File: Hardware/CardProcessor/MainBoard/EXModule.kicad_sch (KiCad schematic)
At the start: 1 part, among them J3 MEC5-140-01-L-DV-W1-K

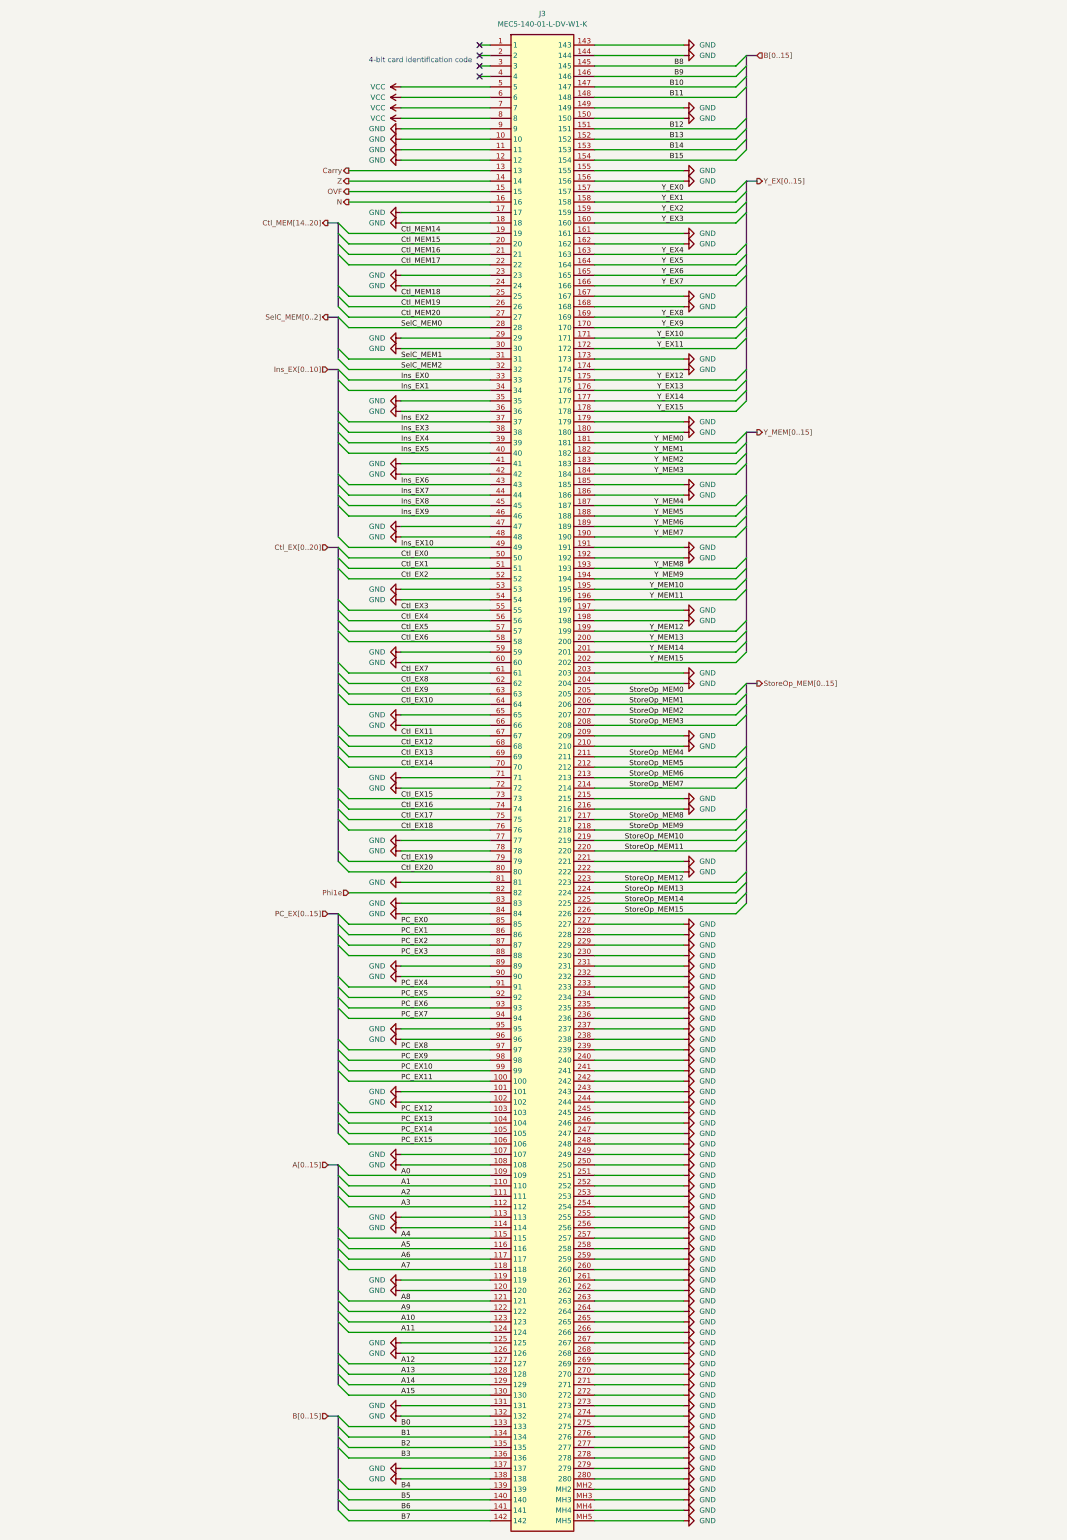
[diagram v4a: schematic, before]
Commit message: MainBoard: Rearrange slot connector pinout for easier PCB routing
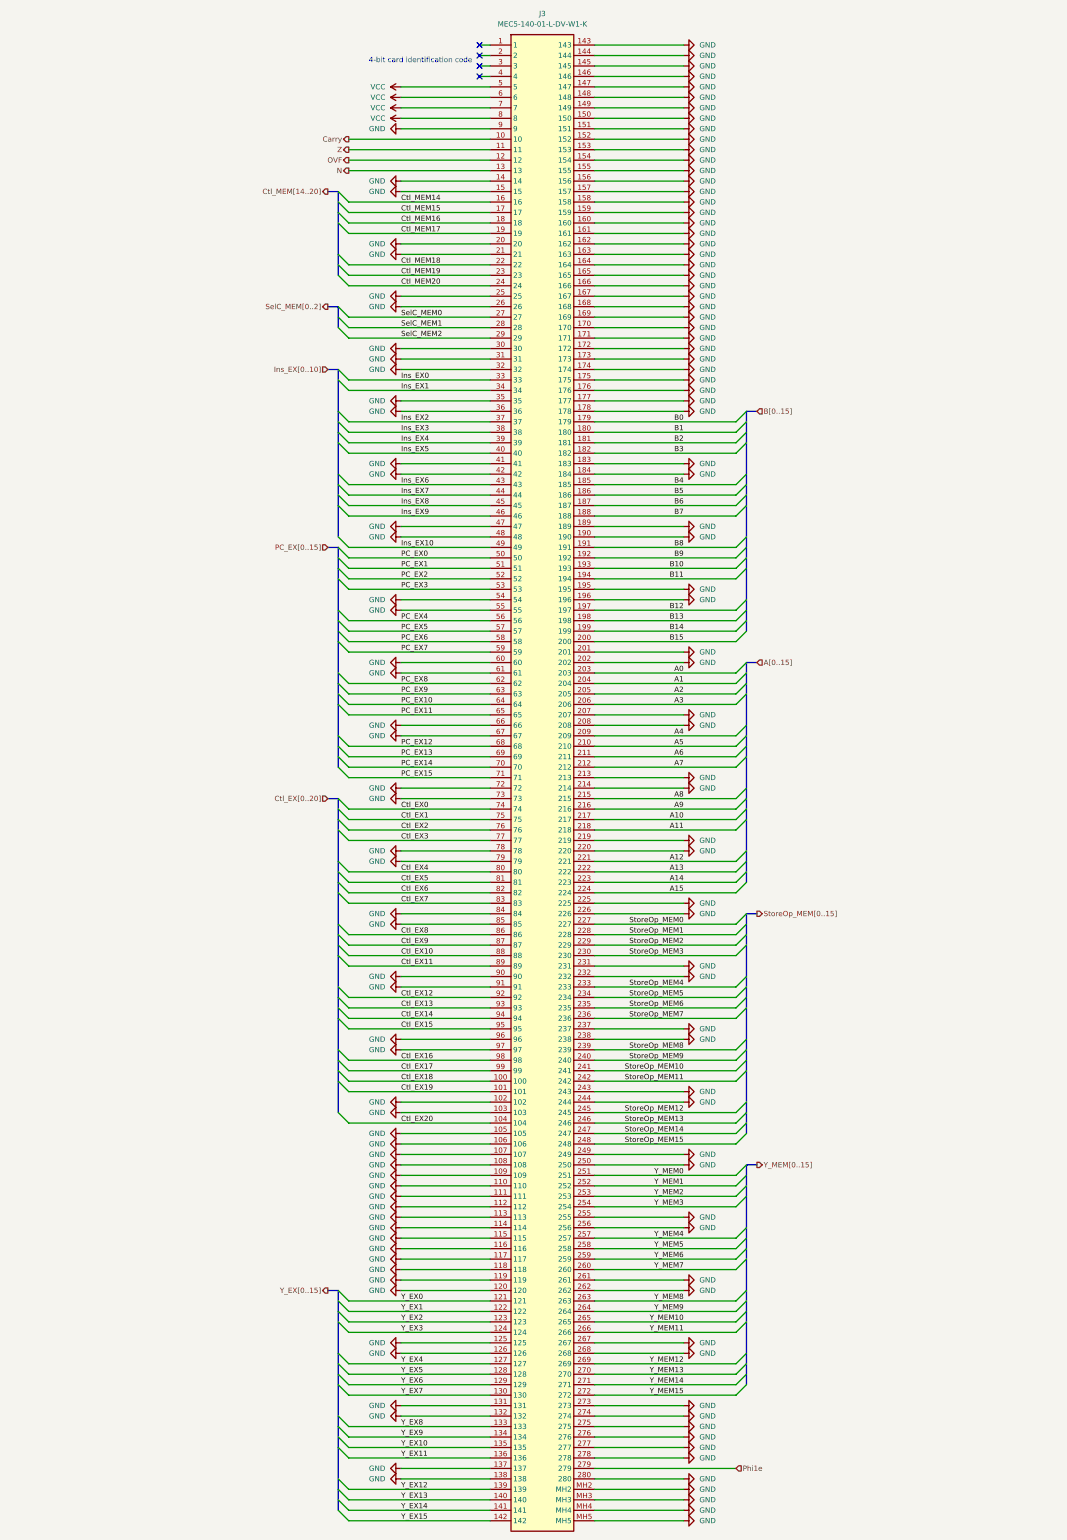
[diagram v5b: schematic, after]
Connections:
- net A0: now also J3.203; no longer J3.109
- net A1: now also J3.204; no longer J3.110
- net A10: now also J3.217; no longer J3.123
- net A11: now also J3.218; no longer J3.124
- net A12: now also J3.221; no longer J3.127
- net A13: now also J3.222; no longer J3.128
- net A14: now also J3.223; no longer J3.129
- net A15: now also J3.224; no longer J3.130
- net A2: now also J3.205; no longer J3.111
- net A3: now also J3.206; no longer J3.112
- net A4: now also J3.209; no longer J3.115
- net A5: now also J3.210; no longer J3.116
- net A6: now also J3.211; no longer J3.117
- net A7: now also J3.212; no longer J3.118
- net A8: now also J3.215; no longer J3.121
- net A9: now also J3.216; no longer J3.122
- net B0: now also J3.179; no longer J3.133
- net B1: now also J3.180; no longer J3.134
- net B10: now also J3.193; no longer J3.147
- net B11: now also J3.194; no longer J3.148
- net B12: now also J3.197; no longer J3.151
- net B13: now also J3.198; no longer J3.152
- net B14: now also J3.199; no longer J3.153
- net B15: now also J3.200; no longer J3.154
- net B2: now also J3.181; no longer J3.135
- net B3: now also J3.182; no longer J3.136
- net B4: now also J3.185; no longer J3.139
- net B5: now also J3.186; no longer J3.140
- net B6: now also J3.187; no longer J3.141
- net B7: now also J3.188; no longer J3.142
- net B8: now also J3.191; no longer J3.145
- net B9: now also J3.192; no longer J3.146
- net Carry: now also J3.10; no longer J3.13
- net Ctl_EX0: now also J3.74; no longer J3.50
- net Ctl_EX1: now also J3.75; no longer J3.51
- net Ctl_EX10: now also J3.88; no longer J3.64
- net Ctl_EX11: now also J3.89; no longer J3.67
- net Ctl_EX12: now also J3.92; no longer J3.68
- net Ctl_EX13: now also J3.93; no longer J3.69
- net Ctl_EX14: now also J3.94; no longer J3.70
- net Ctl_EX15: now also J3.95; no longer J3.73
- net Ctl_EX16: now also J3.98; no longer J3.74
- net Ctl_EX17: now also J3.99; no longer J3.75
- net Ctl_EX18: now also J3.100; no longer J3.76
- net Ctl_EX19: now also J3.101; no longer J3.79
- net Ctl_EX2: now also J3.76; no longer J3.52
- net Ctl_EX20: now also J3.104; no longer J3.80
- net Ctl_EX3: now also J3.77; no longer J3.55
- net Ctl_EX4: now also J3.80; no longer J3.56
- net Ctl_EX5: now also J3.81; no longer J3.57
- net Ctl_EX6: now also J3.82; no longer J3.58
- net Ctl_EX7: now also J3.83; no longer J3.61
- net Ctl_EX8: now also J3.86; no longer J3.62
- net Ctl_EX9: now also J3.87; no longer J3.63
- net Ctl_MEM14: now also J3.16; no longer J3.19
- net Ctl_MEM15: now also J3.17; no longer J3.20
- net Ctl_MEM16: now also J3.18; no longer J3.21
- net Ctl_MEM17: now also J3.19; no longer J3.22
- net Ctl_MEM18: now also J3.22; no longer J3.25
- net Ctl_MEM19: now also J3.23; no longer J3.26
- net Ctl_MEM20: now also J3.24; no longer J3.27
- net GND: now also J3.103, J3.105, J3.106, J3.109, J3.110, J3.111, J3.112, J3.115, J3.116, J3.117, J3.118, J3.14, J3.145, J3.146, J3.147, J3.148, J3.15, J3.151, J3.152, J3.153, J3.154, J3.157, J3.158, J3.159, J3.160, J3.163, J3.164, J3.165, J3.166, J3.169, J3.170, J3.171, J3.172, J3.175, J3.176, J3.177, J3.178, J3.183, J3.184, J3.189, J3.190, J3.195, J3.196, J3.20, J3.201, J3.202, J3.207, J3.208, J3.21, J3.213, J3.214, J3.219, J3.220, J3.225, J3.226, J3.25, J3.26, J3.31, J3.32, J3.55, J3.61, J3.67, J3.73, J3.79, J3.85, J3.91, J3.97; no longer J3.10, J3.101, J3.11, J3.12, J3.17, J3.179, J3.18, J3.180, J3.185, J3.186, J3.191, J3.192, J3.197, J3.198, J3.203, J3.204, J3.209, J3.210, J3.215, J3.216, J3.221, J3.222, J3.227, J3.228, J3.229, J3.23, J3.230, J3.233, J3.234, J3.235, J3.236, J3.239, J3.24, J3.240, J3.241, J3.242, J3.245, J3.246, J3.247, J3.248, J3.251, J3.252, J3.253, J3.254, J3.257, J3.258, J3.259, J3.260, J3.263, J3.264, J3.265, J3.266, J3.269, J3.270, J3.271, J3.272, J3.279, J3.29, J3.53, J3.59, J3.65, J3.71, J3.77, J3.81, J3.83, J3.89, J3.95
- net N: now also J3.13; no longer J3.16
- net OVF: now also J3.12; no longer J3.15
- net PC_EX0: now also J3.50; no longer J3.85
- net PC_EX1: now also J3.51; no longer J3.86
- net PC_EX10: now also J3.64; no longer J3.99
- net PC_EX11: now also J3.65; no longer J3.100
- net PC_EX12: now also J3.68; no longer J3.103
- net PC_EX13: now also J3.69; no longer J3.104
- net PC_EX14: now also J3.70; no longer J3.105
- net PC_EX15: now also J3.71; no longer J3.106
- net PC_EX2: now also J3.52; no longer J3.87
- net PC_EX3: now also J3.53; no longer J3.88
- net PC_EX4: now also J3.56; no longer J3.91
- net PC_EX5: now also J3.57; no longer J3.92
- net PC_EX6: now also J3.58; no longer J3.93
- net PC_EX7: now also J3.59; no longer J3.94
- net PC_EX8: now also J3.62; no longer J3.97
- net PC_EX9: now also J3.63; no longer J3.98
- net Phi1e: now also J3.279; no longer J3.82
- net SelC_MEM0: now also J3.27; no longer J3.28
- net SelC_MEM1: now also J3.28; no longer J3.31
- net SelC_MEM2: now also J3.29; no longer J3.32
- net StoreOp_MEM0: now also J3.227; no longer J3.205
- net StoreOp_MEM1: now also J3.228; no longer J3.206
- net StoreOp_MEM10: now also J3.241; no longer J3.219
- net StoreOp_MEM11: now also J3.242; no longer J3.220
- net StoreOp_MEM12: now also J3.245; no longer J3.223
- net StoreOp_MEM13: now also J3.246; no longer J3.224
- net StoreOp_MEM14: now also J3.247; no longer J3.225
- net StoreOp_MEM15: now also J3.248; no longer J3.226
- net StoreOp_MEM2: now also J3.229; no longer J3.207
- net StoreOp_MEM3: now also J3.230; no longer J3.208
- net StoreOp_MEM4: now also J3.233; no longer J3.211
- net StoreOp_MEM5: now also J3.234; no longer J3.212
- net StoreOp_MEM6: now also J3.235; no longer J3.213
- net StoreOp_MEM7: now also J3.236; no longer J3.214
- net StoreOp_MEM8: now also J3.239; no longer J3.217
- net StoreOp_MEM9: now also J3.240; no longer J3.218
- net Y_EX0: now also J3.121; no longer J3.157
- net Y_EX1: now also J3.122; no longer J3.158
- net Y_EX10: now also J3.135; no longer J3.171
- net Y_EX11: now also J3.136; no longer J3.172
- net Y_EX12: now also J3.139; no longer J3.175
- net Y_EX13: now also J3.140; no longer J3.176
- net Y_EX14: now also J3.141; no longer J3.177
- net Y_EX15: now also J3.142; no longer J3.178
- net Y_EX2: now also J3.123; no longer J3.159
- net Y_EX3: now also J3.124; no longer J3.160
- net Y_EX4: now also J3.127; no longer J3.163
- net Y_EX5: now also J3.128; no longer J3.164
- net Y_EX6: now also J3.129; no longer J3.165
- net Y_EX7: now also J3.130; no longer J3.166
- net Y_EX8: now also J3.133; no longer J3.169
- net Y_EX9: now also J3.134; no longer J3.170
- net Y_MEM0: now also J3.251; no longer J3.181
- net Y_MEM1: now also J3.252; no longer J3.182
- net Y_MEM10: now also J3.265; no longer J3.195
- net Y_MEM11: now also J3.266; no longer J3.196
- net Y_MEM12: now also J3.269; no longer J3.199
- net Y_MEM13: now also J3.270; no longer J3.200
- net Y_MEM14: now also J3.271; no longer J3.201
- net Y_MEM15: now also J3.272; no longer J3.202
- net Y_MEM2: now also J3.253; no longer J3.183
- net Y_MEM3: now also J3.254; no longer J3.184
- net Y_MEM4: now also J3.257; no longer J3.187
- net Y_MEM5: now also J3.258; no longer J3.188
- net Y_MEM6: now also J3.259; no longer J3.189
- net Y_MEM7: now also J3.260; no longer J3.190
- net Y_MEM8: now also J3.263; no longer J3.193
- net Y_MEM9: now also J3.264; no longer J3.194
- net Z: now also J3.11; no longer J3.14

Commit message: MainBoard: Change card slots' pinout to ease routing of the PCB
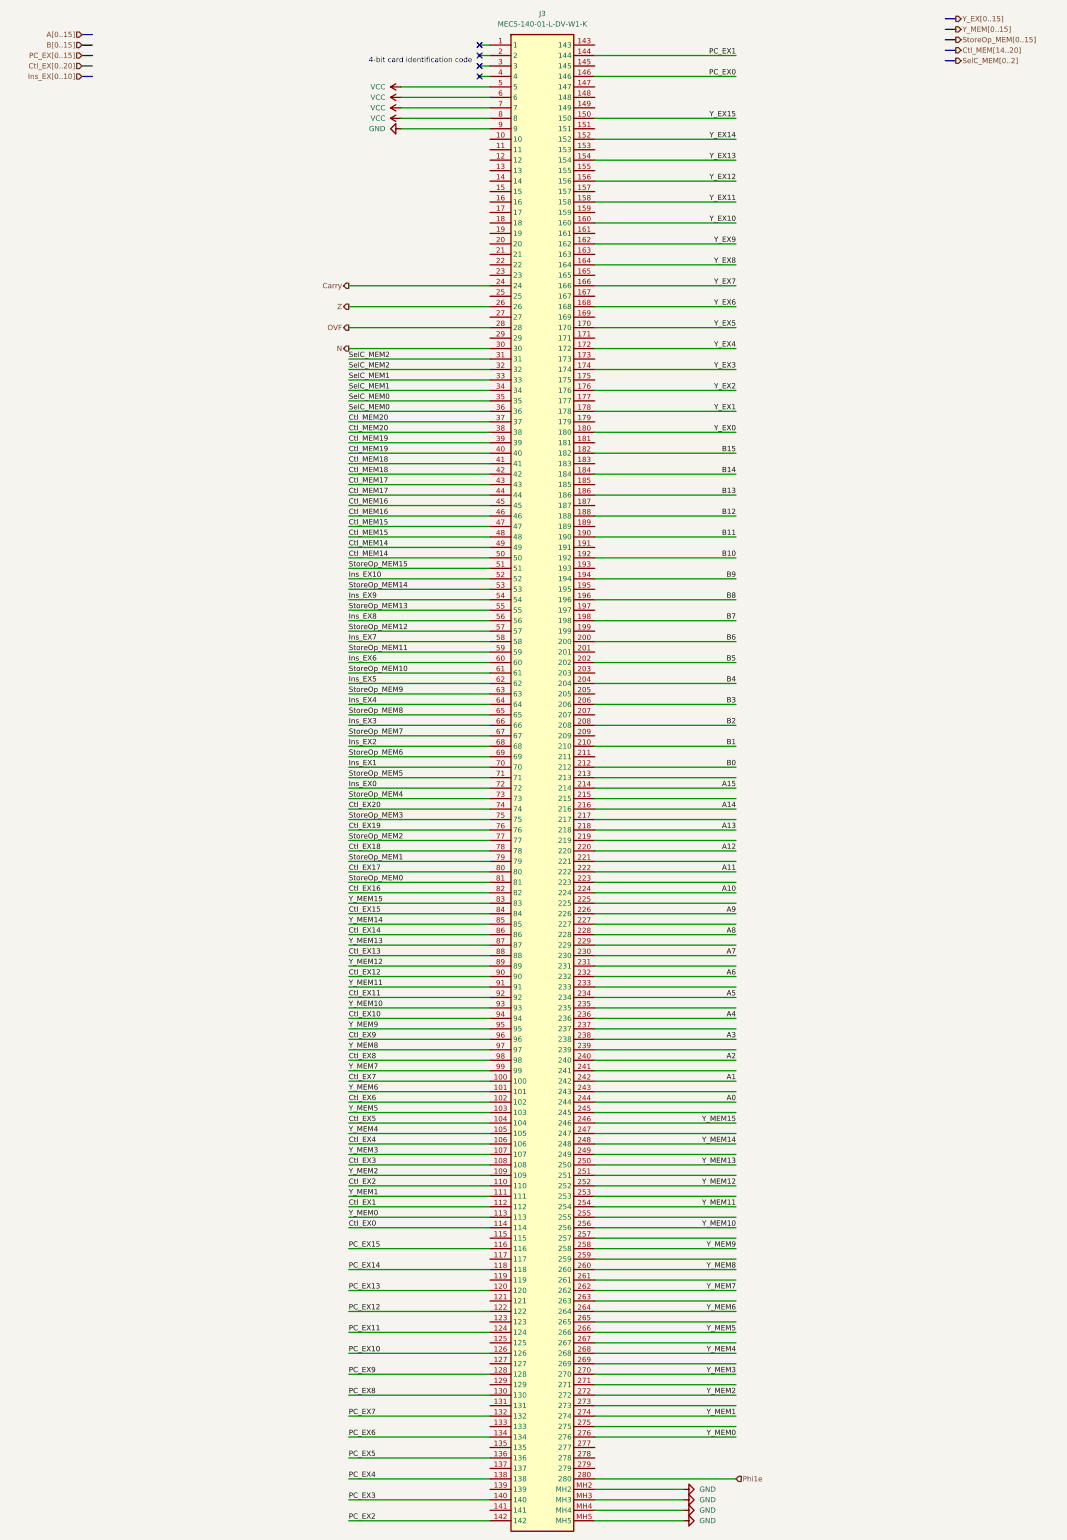
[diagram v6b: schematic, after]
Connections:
- net A0: now also J3.244; no longer J3.203
- net A1: now also J3.242; no longer J3.204
- net A10: now also J3.224; no longer J3.217
- net A11: now also J3.222; no longer J3.218
- net A12: now also J3.220; no longer J3.221
- net A13: now also J3.218; no longer J3.222
- net A14: now also J3.216; no longer J3.223
- net A15: now also J3.214; no longer J3.224
- net A2: now also J3.240; no longer J3.205
- net A3: now also J3.238; no longer J3.206
- net A4: now also J3.236; no longer J3.209
- net A5: now also J3.234; no longer J3.210
- net A6: now also J3.232; no longer J3.211
- net A7: now also J3.230; no longer J3.212
- net A8: now also J3.228; no longer J3.215
- net A9: now also J3.226; no longer J3.216
- net B0: now also J3.212; no longer J3.179
- net B1: now also J3.210; no longer J3.180
- net B10: now also J3.192; no longer J3.193
- net B11: now also J3.190; no longer J3.194
- net B12: now also J3.188; no longer J3.197
- net B13: now also J3.186; no longer J3.198
- net B14: now also J3.184; no longer J3.199
- net B15: now also J3.182; no longer J3.200
- net B2: now also J3.208; no longer J3.181
- net B3: now also J3.206; no longer J3.182
- net B4: now also J3.204; no longer J3.185
- net B5: now also J3.202; no longer J3.186
- net B6: now also J3.200; no longer J3.187
- net B7: now also J3.198; no longer J3.188
- net B8: now also J3.196; no longer J3.191
- net B9: now also J3.194; no longer J3.192
- net Carry: now also J3.24; no longer J3.10
- net Ctl_EX0: now also J3.114; no longer J3.74
- net Ctl_EX1: now also J3.112; no longer J3.75
- net Ctl_EX10: now also J3.94; no longer J3.88
- net Ctl_EX11: now also J3.92; no longer J3.89
- net Ctl_EX12: now also J3.90; no longer J3.92
- net Ctl_EX13: now also J3.88; no longer J3.93
- net Ctl_EX14: now also J3.86; no longer J3.94
- net Ctl_EX15: now also J3.84; no longer J3.95
- net Ctl_EX16: now also J3.82; no longer J3.98
- net Ctl_EX17: now also J3.80; no longer J3.99
- net Ctl_EX18: now also J3.78; no longer J3.100
- net Ctl_EX19: now also J3.76; no longer J3.101
- net Ctl_EX2: now also J3.110; no longer J3.76
- net Ctl_EX20: now also J3.74; no longer J3.104
- net Ctl_EX3: now also J3.108; no longer J3.77
- net Ctl_EX4: now also J3.106; no longer J3.80
- net Ctl_EX5: now also J3.104; no longer J3.81
- net Ctl_EX6: now also J3.102; no longer J3.82
- net Ctl_EX7: now also J3.100; no longer J3.83
- net Ctl_EX8: now also J3.98; no longer J3.86
- net Ctl_EX9: now also J3.96; no longer J3.87
- net Ctl_MEM14: now also J3.49, J3.50; no longer J3.16
- net Ctl_MEM15: now also J3.47, J3.48; no longer J3.17
- net Ctl_MEM16: now also J3.45, J3.46; no longer J3.18
- net Ctl_MEM17: now also J3.43, J3.44; no longer J3.19
- net Ctl_MEM18: now also J3.41, J3.42; no longer J3.22
- net Ctl_MEM19: now also J3.39, J3.40; no longer J3.23
- net Ctl_MEM20: now also J3.37, J3.38; no longer J3.24
- net GND: no longer J3.102, J3.103, J3.105, J3.106, J3.107, J3.108, J3.109, J3.110, J3.111, J3.112, J3.113, J3.114, J3.115, J3.116, J3.117, J3.118, J3.119, J3.120, J3.125, J3.126, J3.131, J3.132, J3.137, J3.138, J3.14, J3.143, J3.144, J3.145, J3.146, J3.147, J3.148, J3.149, J3.15, J3.150, J3.151, J3.152, J3.153, J3.154, J3.155, J3.156, J3.157, J3.158, J3.159, J3.160, J3.161, J3.162, J3.163, J3.164, J3.165, J3.166, J3.167, J3.168, J3.169, J3.170, J3.171, J3.172, J3.173, J3.174, J3.175, J3.176, J3.177, J3.178, J3.183, J3.184, J3.189, J3.190, J3.195, J3.196, J3.20, J3.201, J3.202, J3.207, J3.208, J3.21, J3.213, J3.214, J3.219, J3.220, J3.225, J3.226, J3.231, J3.232, J3.237, J3.238, J3.243, J3.244, J3.249, J3.25, J3.250, J3.255, J3.256, J3.26, J3.261, J3.262, J3.267, J3.268, J3.273, J3.274, J3.275, J3.276, J3.277, J3.278, J3.280, J3.30, J3.31, J3.32, J3.35, J3.36, J3.41, J3.42, J3.47, J3.48, J3.54, J3.55, J3.60, J3.61, J3.66, J3.67, J3.72, J3.73, J3.78, J3.79, J3.84, J3.85, J3.90, J3.91, J3.96, J3.97
- net Ins_EX0: now also J3.72; no longer J3.33
- net Ins_EX1: now also J3.70; no longer J3.34
- net Ins_EX10: now also J3.52; no longer J3.49
- net Ins_EX2: now also J3.68; no longer J3.37
- net Ins_EX3: now also J3.66; no longer J3.38
- net Ins_EX4: now also J3.64; no longer J3.39
- net Ins_EX5: now also J3.62; no longer J3.40
- net Ins_EX6: now also J3.60; no longer J3.43
- net Ins_EX7: now also J3.58; no longer J3.44
- net Ins_EX8: now also J3.56; no longer J3.45
- net Ins_EX9: now also J3.54; no longer J3.46
- net N: now also J3.30; no longer J3.13
- net OVF: now also J3.28; no longer J3.12
- net PC_EX0: now also J3.146; no longer J3.50
- net PC_EX1: now also J3.144; no longer J3.51
- net PC_EX10: now also J3.126; no longer J3.64
- net PC_EX11: now also J3.124; no longer J3.65
- net PC_EX12: now also J3.122; no longer J3.68
- net PC_EX13: now also J3.120; no longer J3.69
- net PC_EX14: now also J3.118; no longer J3.70
- net PC_EX15: now also J3.116; no longer J3.71
- net PC_EX2: now also J3.142; no longer J3.52
- net PC_EX3: now also J3.140; no longer J3.53
- net PC_EX4: now also J3.138; no longer J3.56
- net PC_EX5: now also J3.136; no longer J3.57
- net PC_EX6: now also J3.134; no longer J3.58
- net PC_EX7: now also J3.132; no longer J3.59
- net PC_EX8: now also J3.130; no longer J3.62
- net PC_EX9: now also J3.128; no longer J3.63
- net Phi1e: now also J3.280; no longer J3.279
- net SelC_MEM0: now also J3.35, J3.36; no longer J3.27
- net SelC_MEM1: now also J3.33, J3.34; no longer J3.28
- net SelC_MEM2: now also J3.31, J3.32; no longer J3.29
- net StoreOp_MEM0: now also J3.81; no longer J3.227
- net StoreOp_MEM1: now also J3.79; no longer J3.228
- net StoreOp_MEM10: now also J3.61; no longer J3.241
- net StoreOp_MEM11: now also J3.59; no longer J3.242
- net StoreOp_MEM12: now also J3.57; no longer J3.245
- net StoreOp_MEM13: now also J3.55; no longer J3.246
- net StoreOp_MEM14: now also J3.53; no longer J3.247
- net StoreOp_MEM15: now also J3.51; no longer J3.248
- net StoreOp_MEM2: now also J3.77; no longer J3.229
- net StoreOp_MEM3: now also J3.75; no longer J3.230
- net StoreOp_MEM4: now also J3.73; no longer J3.233
- net StoreOp_MEM5: now also J3.71; no longer J3.234
- net StoreOp_MEM6: now also J3.69; no longer J3.235
- net StoreOp_MEM7: now also J3.67; no longer J3.236
- net StoreOp_MEM8: now also J3.65; no longer J3.239
- net StoreOp_MEM9: now also J3.63; no longer J3.240
- net Y_EX0: now also J3.180; no longer J3.121
- net Y_EX1: now also J3.178; no longer J3.122
- net Y_EX10: now also J3.160; no longer J3.135
- net Y_EX11: now also J3.158; no longer J3.136
- net Y_EX12: now also J3.156; no longer J3.139
- net Y_EX13: now also J3.154; no longer J3.140
- net Y_EX14: now also J3.152; no longer J3.141
- net Y_EX15: now also J3.150; no longer J3.142
- net Y_EX2: now also J3.176; no longer J3.123
- net Y_EX3: now also J3.174; no longer J3.124
- net Y_EX4: now also J3.172; no longer J3.127
- net Y_EX5: now also J3.170; no longer J3.128
- net Y_EX6: now also J3.168; no longer J3.129
- net Y_EX7: now also J3.166; no longer J3.130
- net Y_EX8: now also J3.164; no longer J3.133
- net Y_EX9: now also J3.162; no longer J3.134
- net Y_MEM0: now also J3.113, J3.276; no longer J3.251
- net Y_MEM1: now also J3.111, J3.274; no longer J3.252
- net Y_MEM10: now also J3.256, J3.93; no longer J3.265
- net Y_MEM11: now also J3.254, J3.91; no longer J3.266
- net Y_MEM12: now also J3.252, J3.89; no longer J3.269
- net Y_MEM13: now also J3.250, J3.87; no longer J3.270
- net Y_MEM14: now also J3.248, J3.85; no longer J3.271
- net Y_MEM15: now also J3.246, J3.83; no longer J3.272
- net Y_MEM2: now also J3.109, J3.272; no longer J3.253
- net Y_MEM3: now also J3.107, J3.270; no longer J3.254
- net Y_MEM4: now also J3.105, J3.268; no longer J3.257
- net Y_MEM5: now also J3.103, J3.266; no longer J3.258
- net Y_MEM6: now also J3.101, J3.264; no longer J3.259
- net Y_MEM7: now also J3.262, J3.99; no longer J3.260
- net Y_MEM8: now also J3.260, J3.97; no longer J3.263
- net Y_MEM9: now also J3.258, J3.95; no longer J3.264
- net Z: now also J3.26; no longer J3.11
